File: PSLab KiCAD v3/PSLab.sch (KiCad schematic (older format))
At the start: 73 parts, among them CON1 USB-MINI-B, J1 V+, J2 GND, J3 V-, J4 Expansion, J5 PG_Pins, J6 Exp, J7 VR-, J8 ESPROG, J9 VR+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

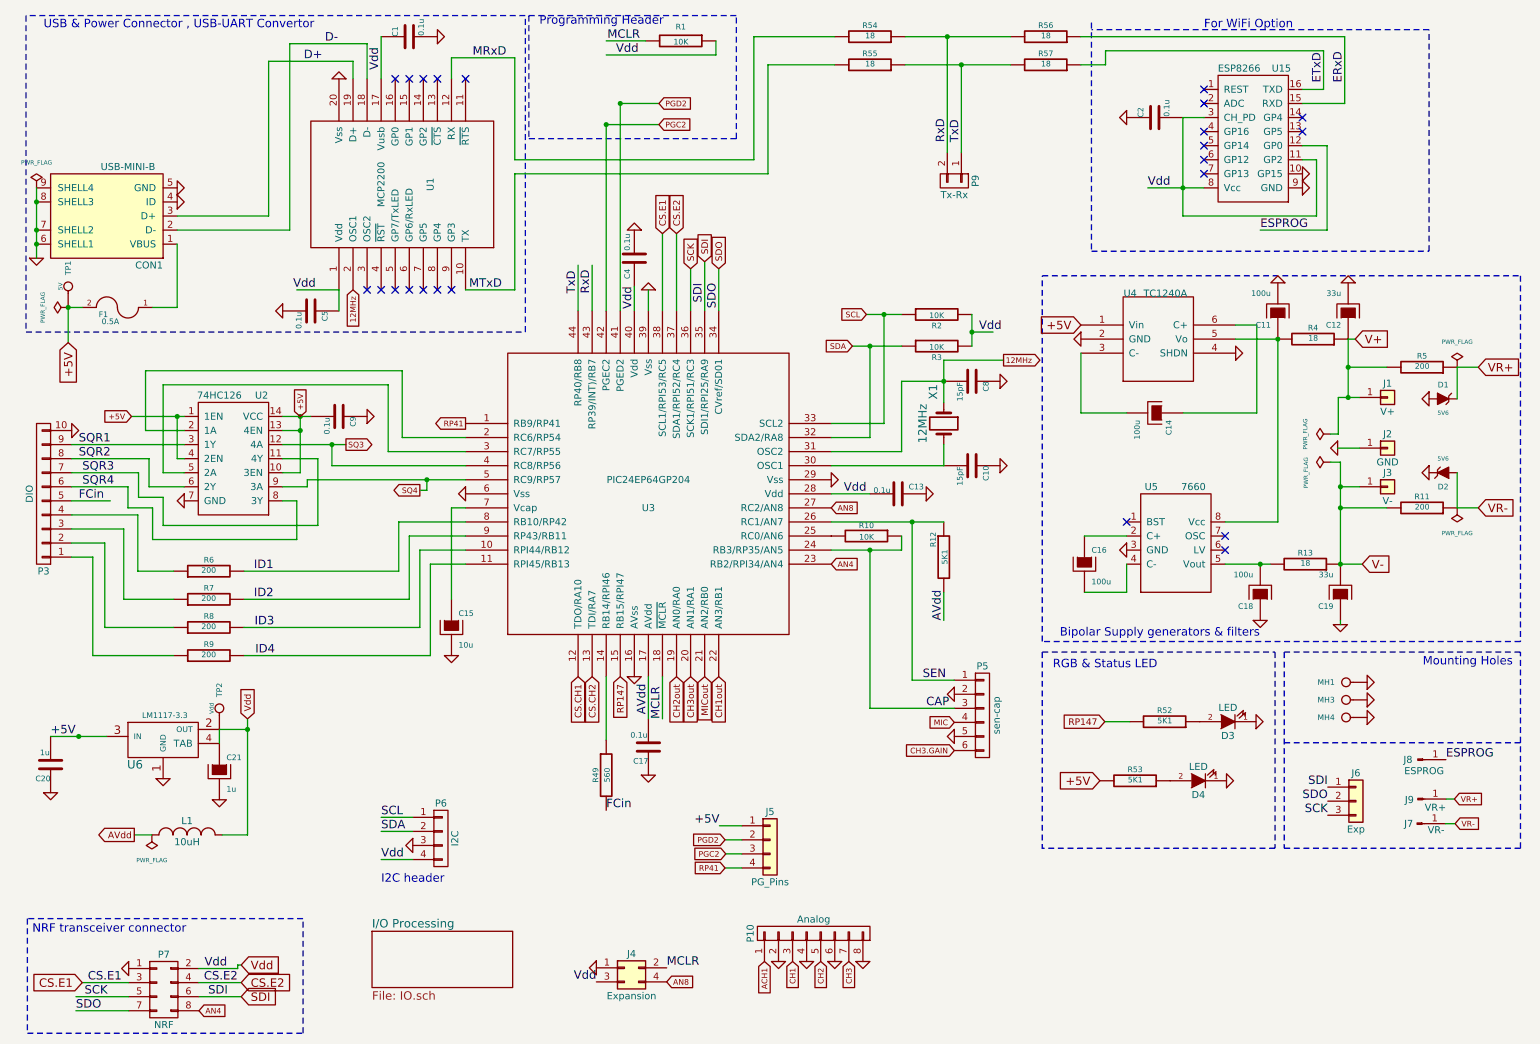
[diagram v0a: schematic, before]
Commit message: Fixes #23 : Replaced USB port with USB Micro B type (#24)
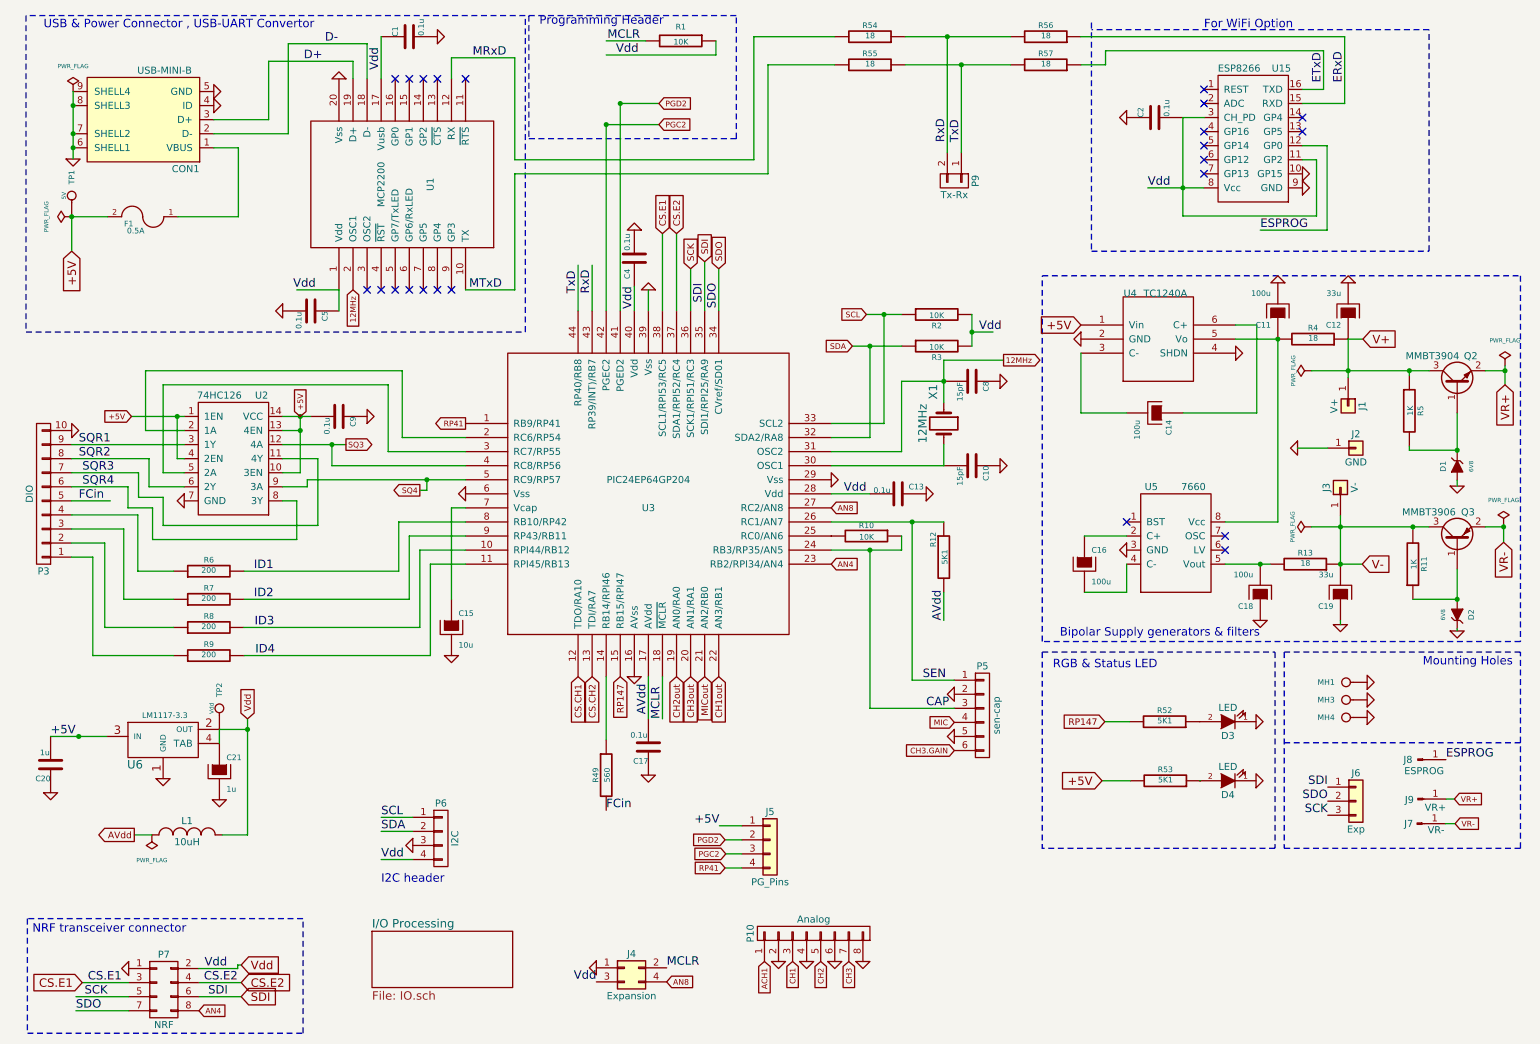
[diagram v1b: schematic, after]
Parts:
- added Q2: MMBT3904, TO_SOT_Packages_SMD:SOT-23, symbol MMBT3904
- added Q3: MMBT3906, TO_SOT_Packages_SMD:SOT-23, symbol MMBT3906
- CON1: footprint Connectors:USB_Mini-B -> Connectors:USB_Micro-B
- D1, D2: value 5V6 -> 6V8
- R11, R5: value 200 -> 1K
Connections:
- wire segments 214 -> 223
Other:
- moved on the sheet: CON1, D1, D2, D4, F1, J1, J2, J3, R11, R5, R53, TP1

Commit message: Added Gerber files
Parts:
- removed J4: Expansion, Pin_Headers:Pin_Header_Straight_2x02_Pitch2.54mm, symbol Conn_02x02_Odd_Even
- removed J8: ESPROG, Pin_Headers:Pin_Header_Straight_1x01_Pitch2.54mm, symbol Conn_01x01_Male
- removed P6: I2C, Pin_Headers:Pin_Header_Straight_2x02_Pitch2.54mm, symbol CONN_01X04
- removed P9: Tx-Rx, Pin_Headers:Pin_Header_Straight_2x01_Pitch2.54mm, symbol CONN_01X02
- added J10: I2C-I, Pin_Headers:Pin_Header_Straight_1x02_Pitch2.54mm, symbol Conn_01x02
- added J11: I2C-II, Pin_Headers:Pin_Header_Straight_1x02_Pitch2.54mm, symbol Conn_01x02
- added J12: Ex-II, Pin_Headers:Pin_Header_Straight_1x02_Pitch2.54mm, symbol Conn_01x02
- added J4: Ex-I, Pin_Headers:Pin_Header_Straight_1x02_Pitch2.54mm, symbol Conn_01x02
- added J8: TX_RX_ES, Pin_Headers:Pin_Header_Straight_1x03_Pitch2.54mm, symbol Conn_01x03
- C12, C19: footprint Capacitors_Tantalum_SMD:CP_Tantalum_Case-A_EIA-3216-18_Reflow -> Capacitors_Tantalum_SMD:CP_Tantalum_Case-B_EIA-3528-21_Reflow
- C21: value 1u -> 10u
- CON1: value USB-MINI-B -> USB-MICRO-B
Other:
- note added: "Status LED"
- note removed: "RGB & Status LED"
- moved on the sheet: J7, J9, MH1, MH3, MH4, R1

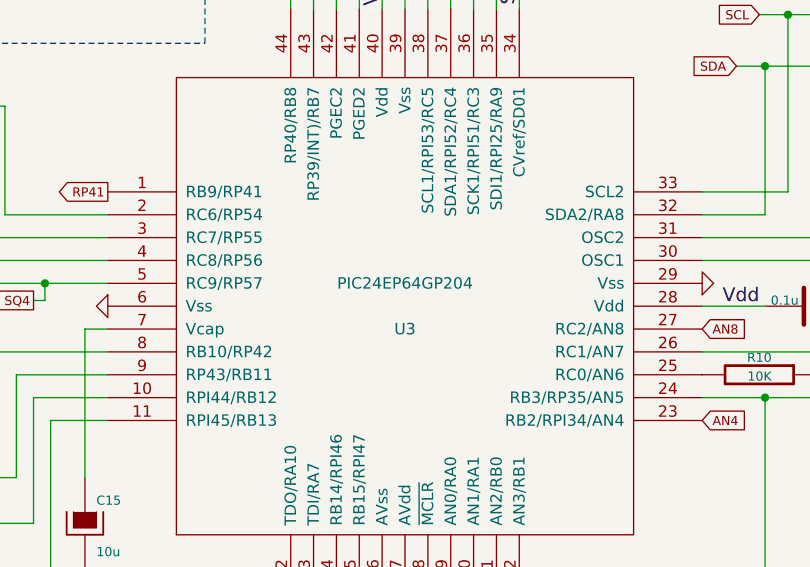
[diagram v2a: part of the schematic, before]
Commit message: Fixes #27 : Replaced microcontroller
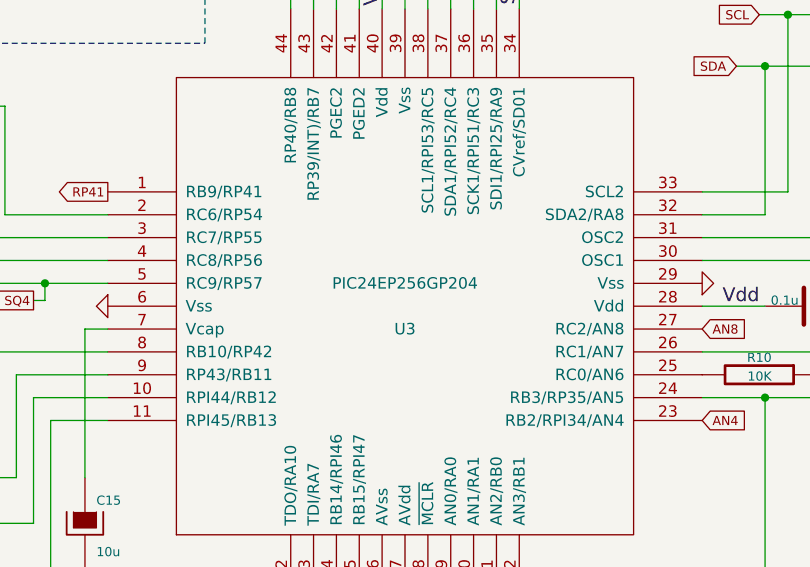
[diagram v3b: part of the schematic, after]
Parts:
- U3: value PIC24EP64GP204 -> PIC24EP256GP204
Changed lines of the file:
@@
 P 4950 3900
 F 0 "U3" H 4950 3800 50  0000 C CNN
-F 1 "PIC24EP64GP204" H 4950 4000 50  0000 C CNN
+F 1 "PIC24EP256GP204" H 4950 4000 50  0000 C CNN
 F 2 "Housings_QFP:TQFP-44_10x10mm_Pitch0.8mm" H 4950 3900 50  0001 C CNN
 F 3 "DOCUMENTATION" H 4950 3900 50  0001 C CNN
